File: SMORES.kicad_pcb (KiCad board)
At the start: 4 copper layers, 20 x 26.8 mm, 40 parts, among them J1 USB_C_Receptacle_USB2.0_14P, SW1 Power, SW2 Reset, SW3 SW0, U2 BQ24075RGT, U3 ICM45686, U4 XC6220B331MR, U5 1532H, U6 QMC6309, U7 E73-2G4M08S1C, Y2 32.768kHz

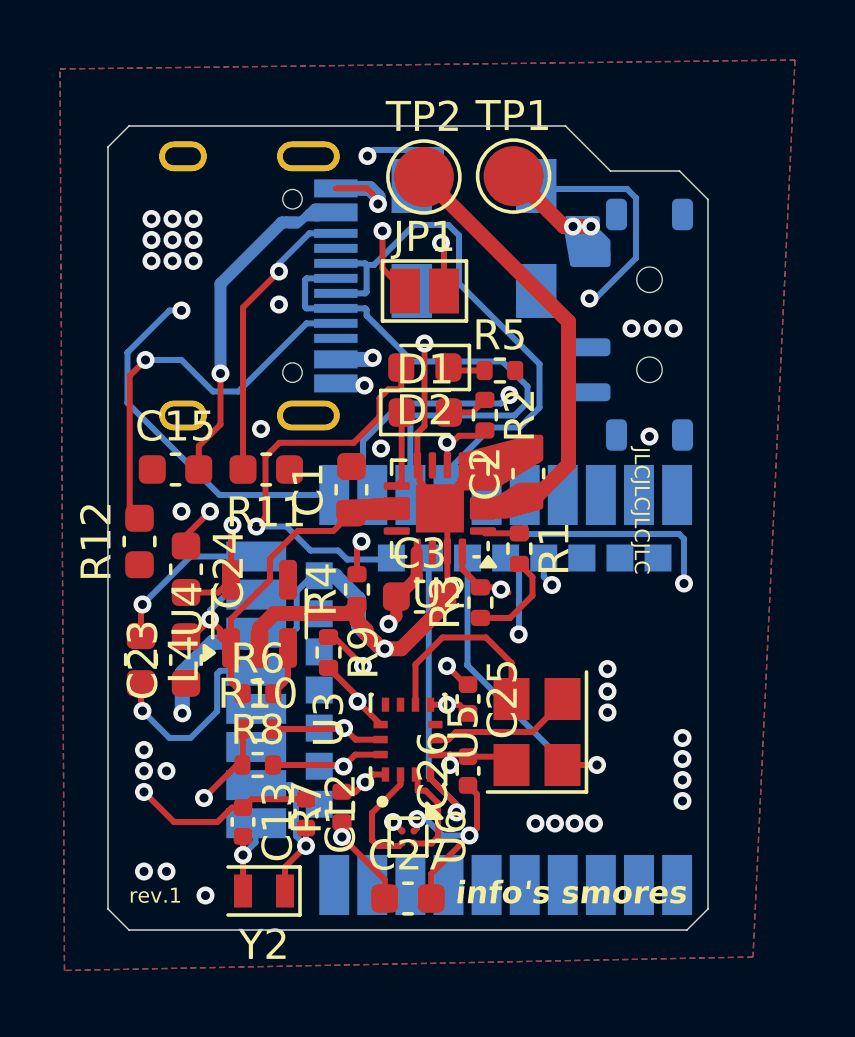
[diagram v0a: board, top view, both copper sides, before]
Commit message: Remove LDO and peripherals
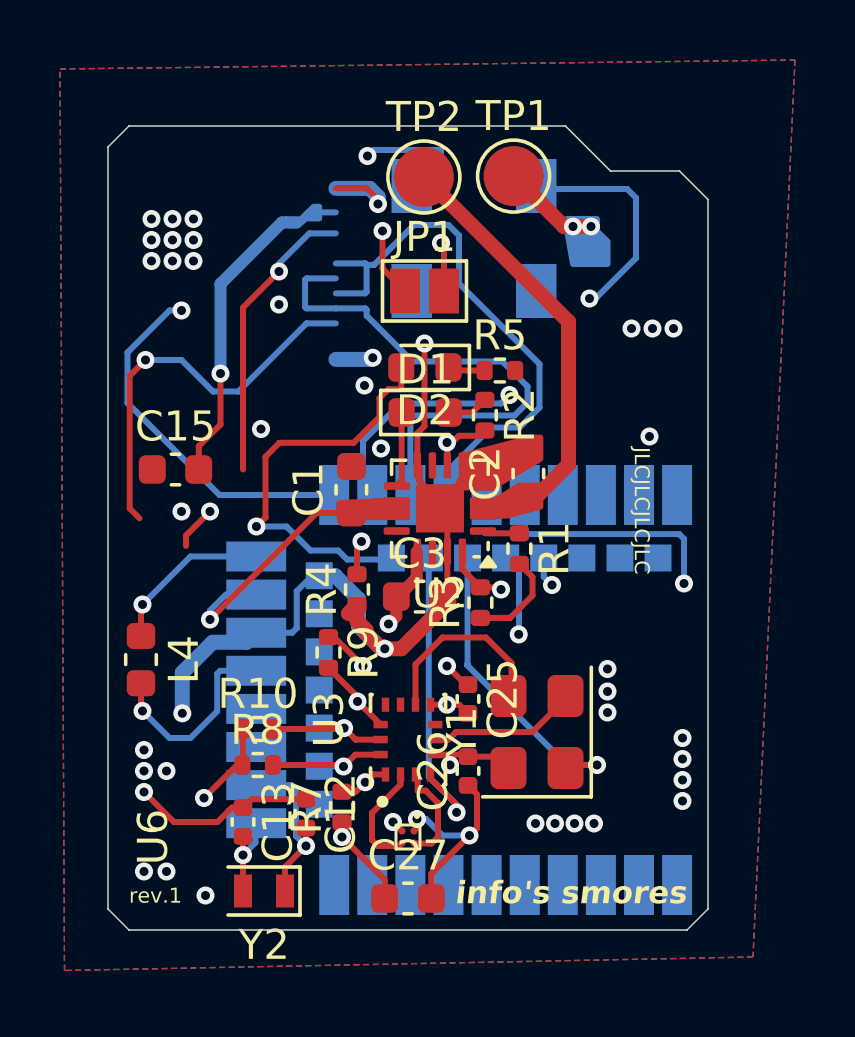
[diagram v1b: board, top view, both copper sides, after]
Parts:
- removed C23, C24: 10uF, Capacitor_SMD:C_0603_1608Metric
- removed J1: USB_C_Receptacle_USB2.0_14P, Connector_USB:USB_C_Receptacle_HRO_TYPE-C-31-M-12
- removed R11, R12: 5.1k, Capacitor_SMD:C_0603_1608Metric
- removed R6: 10M, Resistor_SMD:R_0402_1005Metric
- removed SW1: Power, SMORES:SW_SPDT_Shouhan_MSK12C02
- removed U4: XC6220B331MR, Package_TO_SOT_SMD:SOT-23-5
- removed U5: 1532H, Crystal:Crystal_SMD_3225-4Pin_3.2x2.5mm
- added Y1: SG-8002CE, Oscillator:Oscillator_SMD_SeikoEpson_SG8002CE-4Pin_3.2x2.5mm, F.Cu at (179.5, 95.2)
- U3: footprint ICM_SLIME:IC_ICM-45686 -> ICM-45686:IC_ICM-45686
- U6: footprint Custom:WLCSP-4_0.8x0.8mm_Layout2x2_P0.4mm -> QMC6309:IC_QMC6309
- turned U6 to 90 degrees
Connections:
- TP1 pad 1: Net-(SW1-A) -> GND
- U7 pad 29: D- -> unconnected-(U7-D--Pad29)
- U7 pad 31: D+ -> unconnected-(U7-D+-Pad31)
- U7 pad 9: unconnected-(U7-P0.31/AIN7-Pad9) -> +3V3
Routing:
- net (no net): track 0.00 -> 23.0 mm, vias 0 -> 2
- net unconnected-(U7-D+-Pad31): track 0.00 -> 18.3 mm
- net D+: track 18.3 -> 0.00 mm
- net unconnected-(U7-D--Pad29): track 0.00 -> 17.8 mm
- net D-: track 17.8 -> 0.00 mm
- net Net-(J1-CC1): track 13.3 -> 0.00 mm, vias 1 -> 0
- net Net-(J1-CC2): track 9.67 -> 0.00 mm, vias 1 -> 0
- net VDDH: track 29.2 -> 24.5 mm
- net +3V3: track 27.5 -> 24.0 mm, vias 7 -> 6
- net Net-(SW1-A): track 3.28 -> 0.00 mm, vias 2 -> 0
- net Net-(U4-CE): track 1.73 -> 0.00 mm
- net GND: track 78.3 -> 77.8 mm, vias 44 -> 46

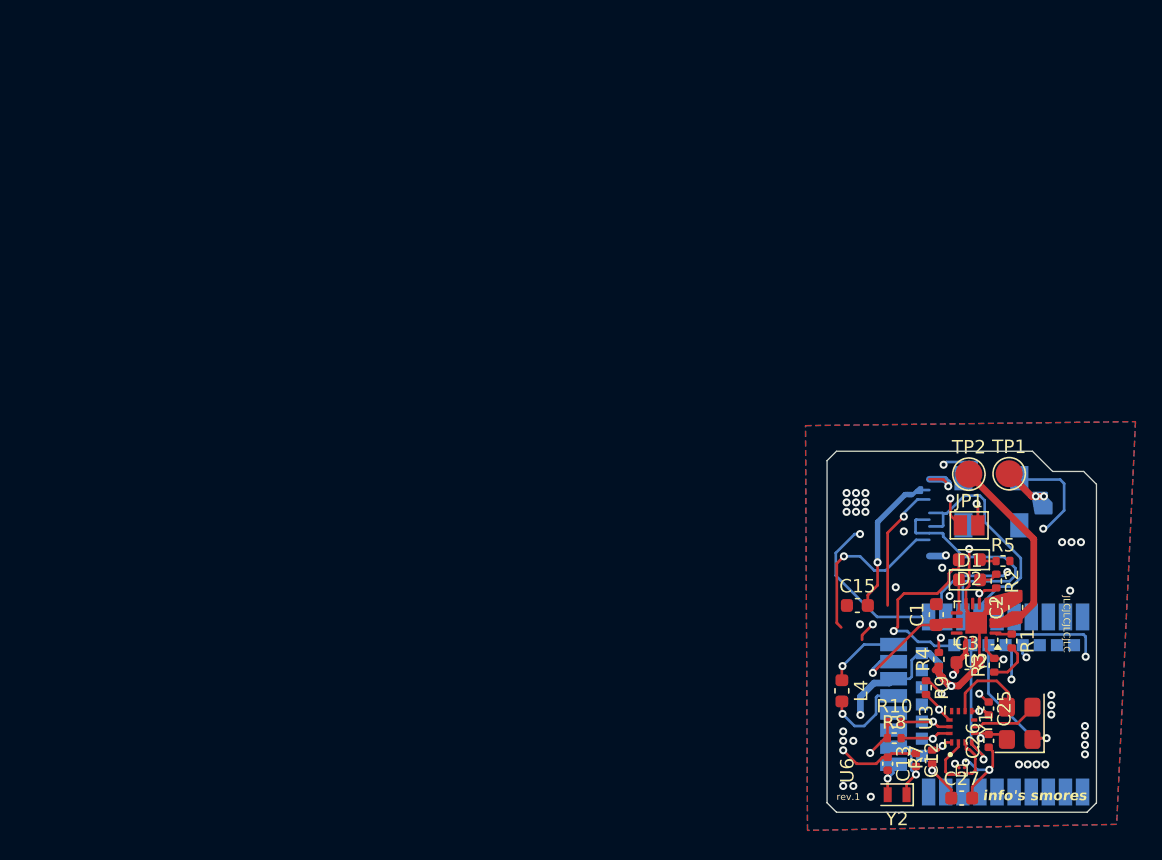
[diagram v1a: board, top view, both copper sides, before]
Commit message: Redesign entire PCB and make it smaller
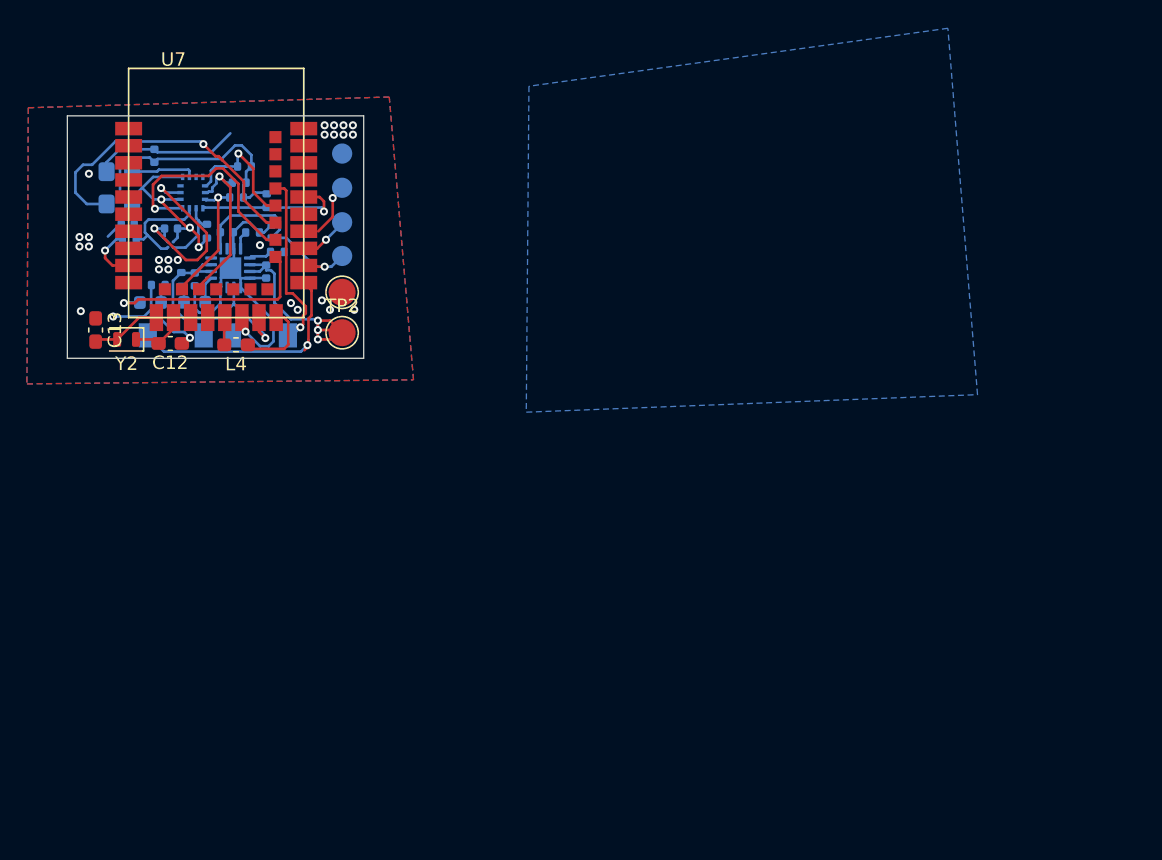
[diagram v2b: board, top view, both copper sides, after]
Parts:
- removed JP1: Big_BAT, Jumper:SolderJumper-2_P1.3mm_Open_Pad1.0x1.5mm
- added R6: 10k, Resistor_SMD:R_0402_1005Metric, B.Cu at (119.2, 58.7)
- added TP3: TestPoint, TestPoint:TestPoint_Pad_D1.5mm, B.Cu at (129.2, 52.9)
- added TP4: TestPoint, TestPoint:TestPoint_Pad_D1.5mm, B.Cu at (129.2, 55.4)
- added TP5: TestPoint, TestPoint:TestPoint_Pad_D1.5mm, B.Cu at (129.2, 58.0)
- added TP6: TestPoint, TestPoint:TestPoint_Pad_D1.5mm, B.Cu at (129.2, 60.5)
- C1, C15, C2, C27, C3: footprint Capacitor_SMD:C_0603_1608Metric -> Capacitor_SMD:C_0402_1005Metric; moved to B.Cu
- C12, C13: footprint Capacitor_SMD:C_0402_1005Metric -> Capacitor_SMD:C_0603_1608Metric_Pad1.08x0.95mm_HandSolder
- C25, C26, D1, D2, R1, R2, R5, U2, U3, U6, Y1: moved to B.Cu
- L4: footprint Inductor_SMD:L_0603_1608Metric -> Inductor_SMD:L_0603_1608Metric_Pad1.05x0.95mm_HandSolder
- R10, R7, R8, R9: value 10k -> 4.7k; moved to B.Cu
- R3, R4: value 11k -> 10k; moved to B.Cu
- U7: moved to F.Cu
- moved Y1 77.8 mm to (112.7, 55.4)
- moved C26 74.5 mm to (113.3, 58.1), turned to 0 degrees
- moved C25 74.3 mm to (115.3, 53.1)
- moved C27 72.3 mm to (116.5, 58.5), turned to 180 degrees
- moved U6 70.5 mm to (116.5, 59.7)
- moved U7 70.3 mm to (119.8, 56.1), turned to 0 degrees
- moved U3 69.5 mm to (118.1, 55.8)
- moved R4 67.7 mm to (113.4, 59.3), turned to 0 degrees
- moved C13 67.0 mm to (110.9, 66.0)
- moved Y2 66.4 mm to (113.2, 66.7)
- moved R5 66.0 mm to (115.6, 62.7), turned to 180 degrees
- moved R2 64.5 mm to (117.3, 62.2), turned to 90 degrees
- moved R7 64.4 mm to (123.6, 56.4), turned to -90 degrees
- moved R3 63.7 mm to (122.6, 58.8), turned to 180 degrees
- moved D2 63.7 mm to (115.0, 64.0)
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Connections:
- R4 pad 1: GND -> +3V3
- R4 pad 2: Net-(JP1-A) -> SCX
- U7 pad 29: unconnected-(U7-D--Pad29) -> D-
- U7 pad 31: unconnected-(U7-D+-Pad31) -> D+
- U7 pad 37: SWD -> unconnected-(U7-SWDIO-Pad37)
- U7 pad 39: SWC -> unconnected-(U7-SWDCLK-Pad39)
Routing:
- net VBUS: track 62.5 -> 16.1 mm, vias 4 -> 1
- net Net-(U2-ISET): track 26.9 -> 1.36 mm, vias 2 -> 0
- net (no net): track 23.0 -> 0.00 mm, vias 2 -> 0
- net Net-(JP1-A): track 20.4 -> 0.00 mm, vias 2 -> 0
- net +3V3: track 24.0 -> 42.6 mm, vias 6 -> 4
- net unconnected-(U7-D+-Pad31): track 18.3 -> 0.00 mm
- net unconnected-(U7-D--Pad29): track 17.8 -> 0.00 mm
- net GND: track 77.8 -> 61.4 mm, vias 46 -> 30
- net SDO: track 26.6 -> 11.5 mm, vias 2 -> 1
- net CLK_CTL: track 10.4 -> 23.7 mm
- net RESET: track 29.1 -> 18.5 mm, vias 2 -> 1
- net SCL: track 4.60 -> 12.9 mm
- net INT1: track 10.6 -> 16.9 mm
- net VDDH: track 24.5 -> 18.3 mm, vias 2 -> 1
- net BAT+: track 13.1 -> 18.5 mm, vias 0 -> 3
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- added copper zone on B.Cu, net +3V3
- removed copper zone on In2.Cu, net +3V3
- removed copper zone on In1.Cu, net GND
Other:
- board size 20 x 26.8 mm -> 22 x 18 mm
- copper layers 4 -> 2
- board text added: "SMORES v1"
- board text removed: "info's smores"
- board text removed: "rev.1"

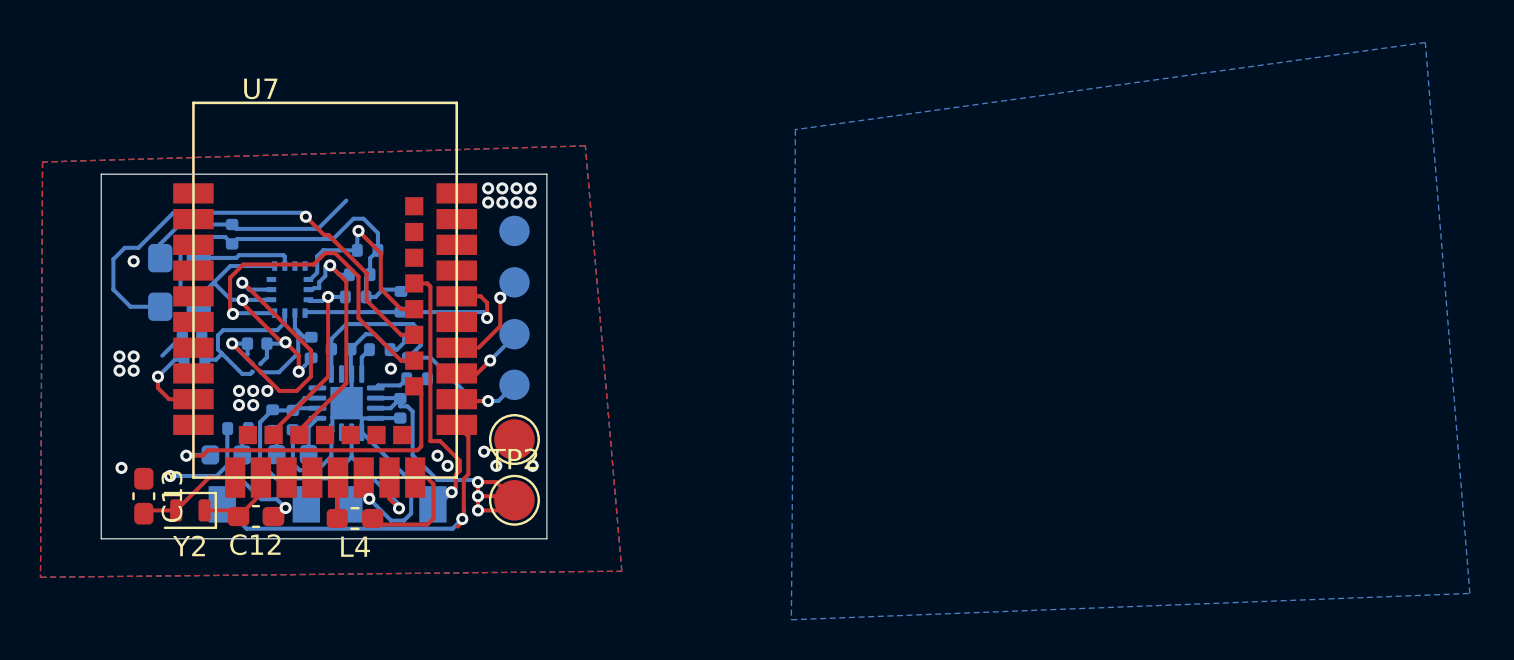
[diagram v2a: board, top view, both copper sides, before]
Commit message: Cleanup design and add silkscreen
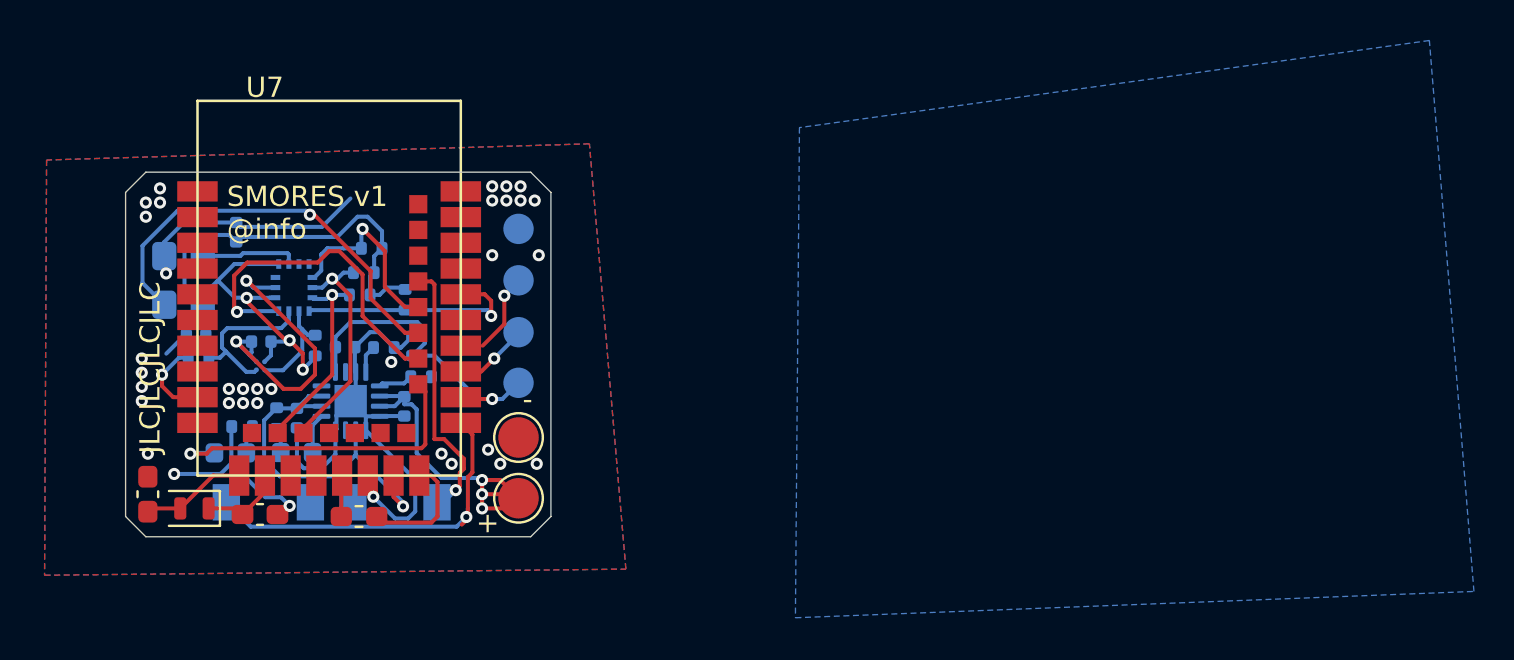
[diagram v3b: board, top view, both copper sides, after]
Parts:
- moved TP2 0.22 mm to (129.4, 66.1)
- moved TP1 0.22 mm to (129.4, 63.1)
- moved TP3 0.22 mm to (129.4, 52.8)
- moved TP5 0.22 mm to (129.4, 57.9)
- moved TP6 0.22 mm to (129.4, 60.4)
- moved TP4 0.22 mm to (129.4, 55.3)
- moved SW2 0.22 mm to (117.0, 66.3)
- moved SW3 0.22 mm to (123.3, 66.3)
- moved Y2 0.22 mm to (113.4, 66.6)
- moved C1 0.22 mm to (118.5, 62.1)
- moved C26 0.22 mm to (113.5, 58.0)
- moved C27 0.22 mm to (116.7, 58.4)
- moved C3 0.22 mm to (120.8, 58.6)
- moved D2 0.22 mm to (115.2, 63.9)
- moved R1 0.22 mm to (124.6, 60.1)
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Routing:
- net CLK_CTL: track 23.7 -> 21.0 mm
- net SCL: track 12.9 -> 11.3 mm
- net GND: vias 30 -> 37
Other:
- board size 22 x 18 mm -> 21 x 18 mm
- board text added: "+"
- board text added: "+5V"
- board text added: "-"
- board text added: "D+"
- board text added: "D-"
- board text added: "GND"
- board text added: "SMORES v1 @info"
- board text removed: "SMORES v1"
